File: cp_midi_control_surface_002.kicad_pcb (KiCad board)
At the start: 2 copper layers, 421.6 x 332.7 mm, 174 parts, among them J1 Conn_02x05_Odd_Even, J2 Conn_02x05_Odd_Even, J7 Conn_02x05_Odd_Even, P1 Power, P11 Guide, P12 Guide, P13 Guide, P2 Analogue, P3 Digital, P4 Communication, P5 PWM, P6 PWM, P8 Guide, P9 Guide, SW1 B3F-5050, SW10 B3F-5050, SW11 B3F-5050, SW12 B3F-5050, SW13 B3F-5050, SW14 B3F-5050, SW15 B3F-5050, SW16 B3F-5050, SW17 B3F-5050, SW18 B3F-5050, SW19 B3F-5050, SW2 B3F-5050, SW20 B3F-5050, SW21 B3F-5050, SW22 B3F-5050, SW23 B3F-5050, SW24 B3F-5050, SW25 B3F-5050, SW26 B3F-5050, SW27 B3F-5050, SW28 B3F-5050, SW29 B3F-5050, SW3 B3F-5050, SW30 B3F-5050, SW31 B3F-5050, SW32 B3F-5050, SW4 B3F-5050, SW41 B3F-5050, SW42 B3F-5050, SW43 B3F-5050, SW44 B3F-5050, SW45 B3F-5050, SW46 B3F-5050, SW47 B3F-5050, SW48 B3F-5050, SW49 B3F-5050, SW5 B3F-5050, SW50 B3F-5050, SW51 B3F-5050, SW52 B3F-5050, SW53 B3F-5050, SW54 B3F-5050, SW55 B3F-5050, SW56 B3F-5050, SW6 B3F-5050, SW7 B3F-5050, SW8 B3F-5050, SW9 B3F-5050, U1 CD74HC4067M, U2 CD74HC4067M, U3 CD74HC4067M, U4 CD74HC4067M, U5 CD74HC4067M, U6 CD74HC4067M

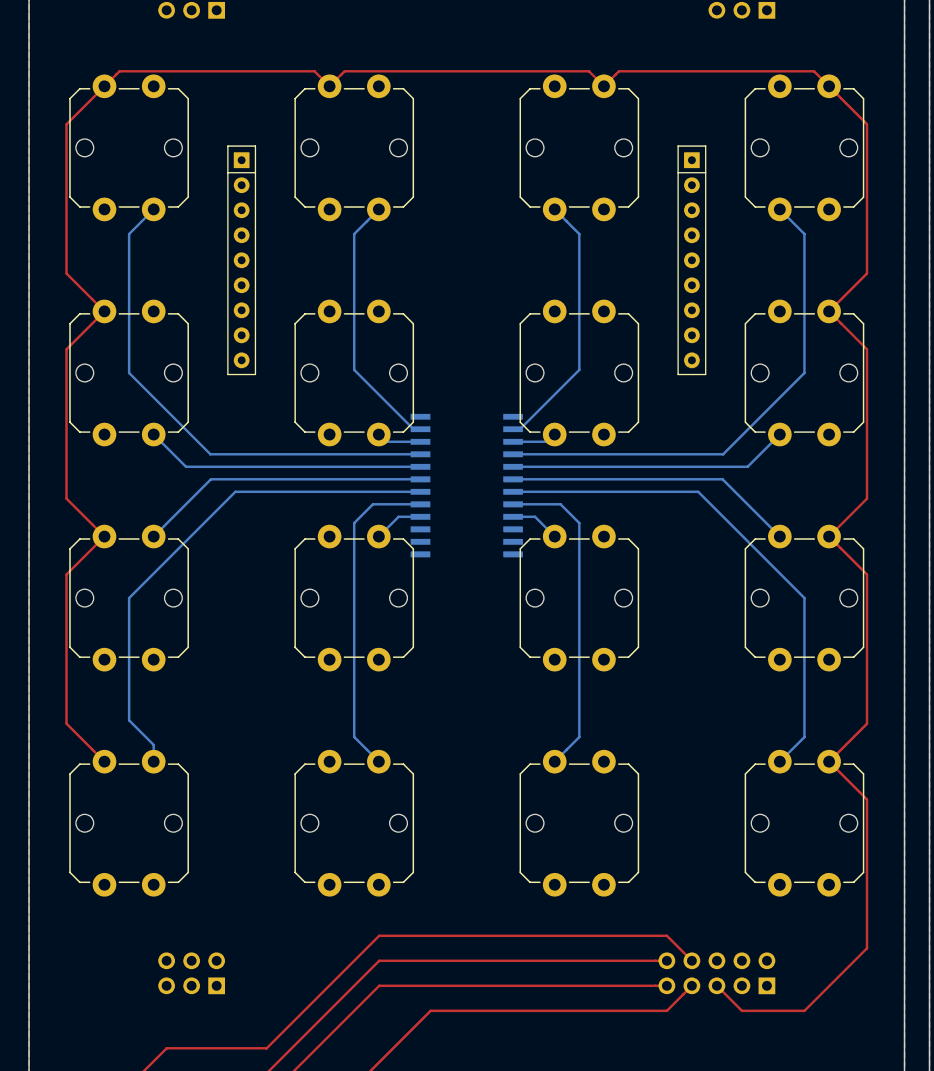
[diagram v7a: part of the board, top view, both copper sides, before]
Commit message: Routing traces on left button block, increased GND plane coverage.
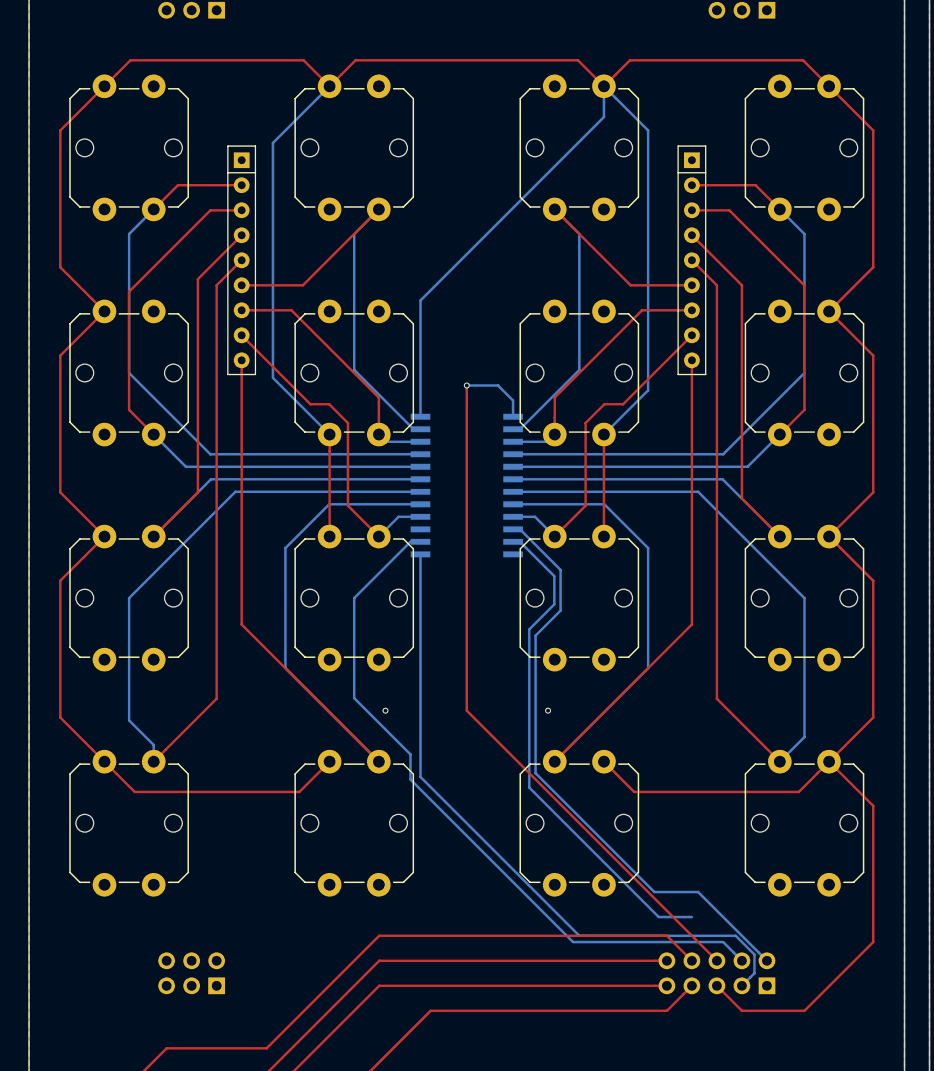
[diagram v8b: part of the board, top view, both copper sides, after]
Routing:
- net +5V: track 1296.5 -> 1495.0 mm
- net Net-(J1-Pad6): track 0.00 -> 75.9 mm, vias 0 -> 1
- net Net-(J1-Pad4): track 0.00 -> 71.2 mm
- net Net-(J1-Pad3): track 0.00 -> 67.7 mm
- net Net-(J1-Pad2): track 0.00 -> 59.6 mm
- net Net-(RN5-Pad9): track 32.8 -> 87.7 mm
- net Net-(RN4-Pad9): track 32.8 -> 87.7 mm
- net Net-(RN5-Pad5): track 51.7 -> 106.3 mm
- net Net-(RN4-Pad5): track 51.7 -> 106.3 mm
- net Net-(J1-Pad1): track 0.00 -> 50.1 mm
- net Net-(RN5-Pad4): track 29.5 -> 63.8 mm
- net Net-(RN4-Pad4): track 29.5 -> 63.8 mm
- net Net-(RN5-Pad3): track 28.4 -> 59.2 mm
- net Net-(RN4-Pad3): track 28.4 -> 58.9 mm
- net Net-(RN4-Pad8): track 5.06 -> 32.4 mm
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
